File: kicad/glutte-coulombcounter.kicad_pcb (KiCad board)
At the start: 2 copper layers, 85 x 50 mm, 59 parts, among them J1 12V, J2 Measure, J3 I2C, J4 AVR-ISP-6, J5 DB9_Female, U1 DS18B20, U2 LT1236-5, U3 LT3433, U4 AD8210, U5 LTC2400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

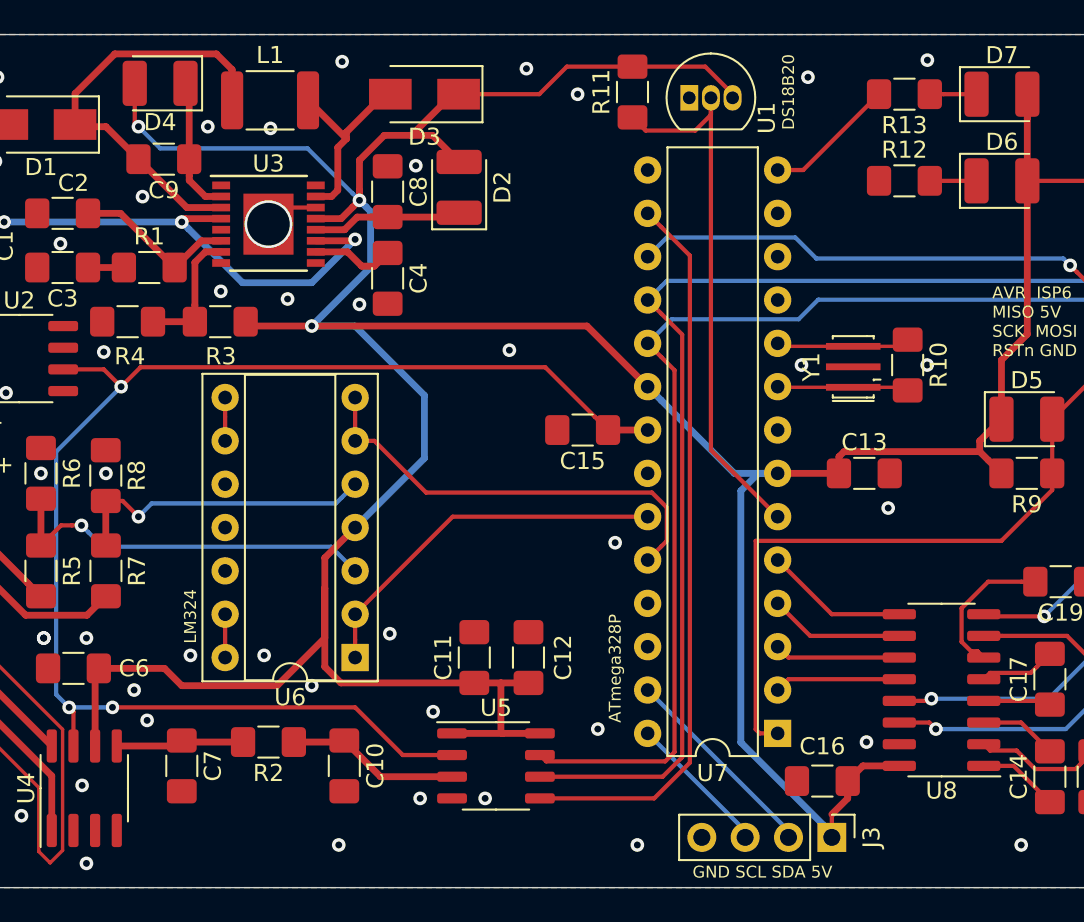
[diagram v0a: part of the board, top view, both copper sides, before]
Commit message: Change LM324 footprint to SOIC
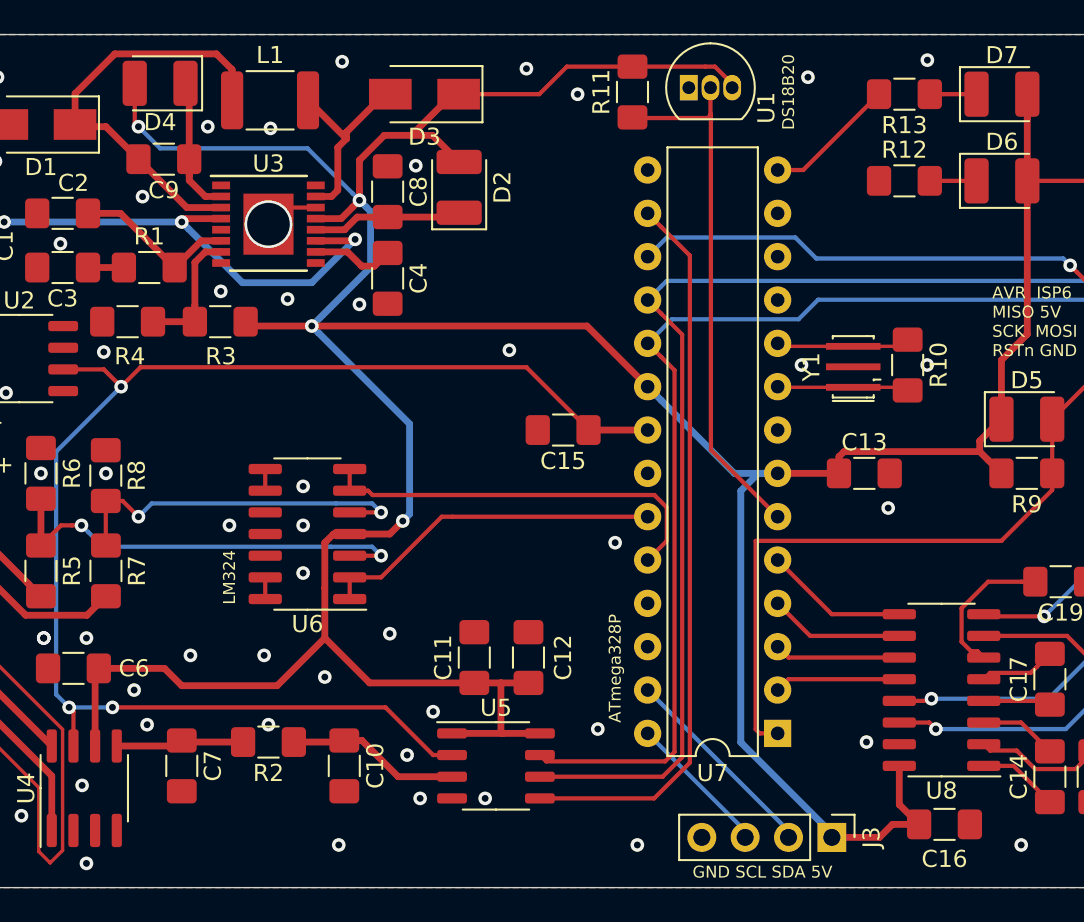
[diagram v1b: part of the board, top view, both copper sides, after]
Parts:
- U6: footprint Package_DIP:DIP-14_W7.62mm_Socket -> Package_SO:SOIC-14_3.9x8.7mm_P1.27mm
- moved U6 7.76 mm to (58.2, 49.3)
- moved C16 7.60 mm to (95.5, 66.3), turned to 0 degrees
- moved C15 1.14 mm to (73.2, 43.2)
- moved U1 0.60 mm to (80.5, 23.1)
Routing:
- net Net-(R7-Pad1): track 18.4 -> 21.5 mm, vias 1 -> 2
- net Net-(R5-Pad1): track 22.7 -> 25.7 mm, vias 1 -> 2
- net /ADC1: track 26.0 -> 23.8 mm
- net +5VA: track 246.7 -> 244.7 mm, vias 3 -> 4
- net /ADC0: track 22.1 -> 20.2 mm
- net Net-(U6-Pad8): track 2.54 -> 1.27 mm
- net Net-(U6-Pad13): track 2.54 -> 1.27 mm
- net /1WIRE: track 32.5 -> 31.5 mm
- net GNDA: vias 60 -> 66

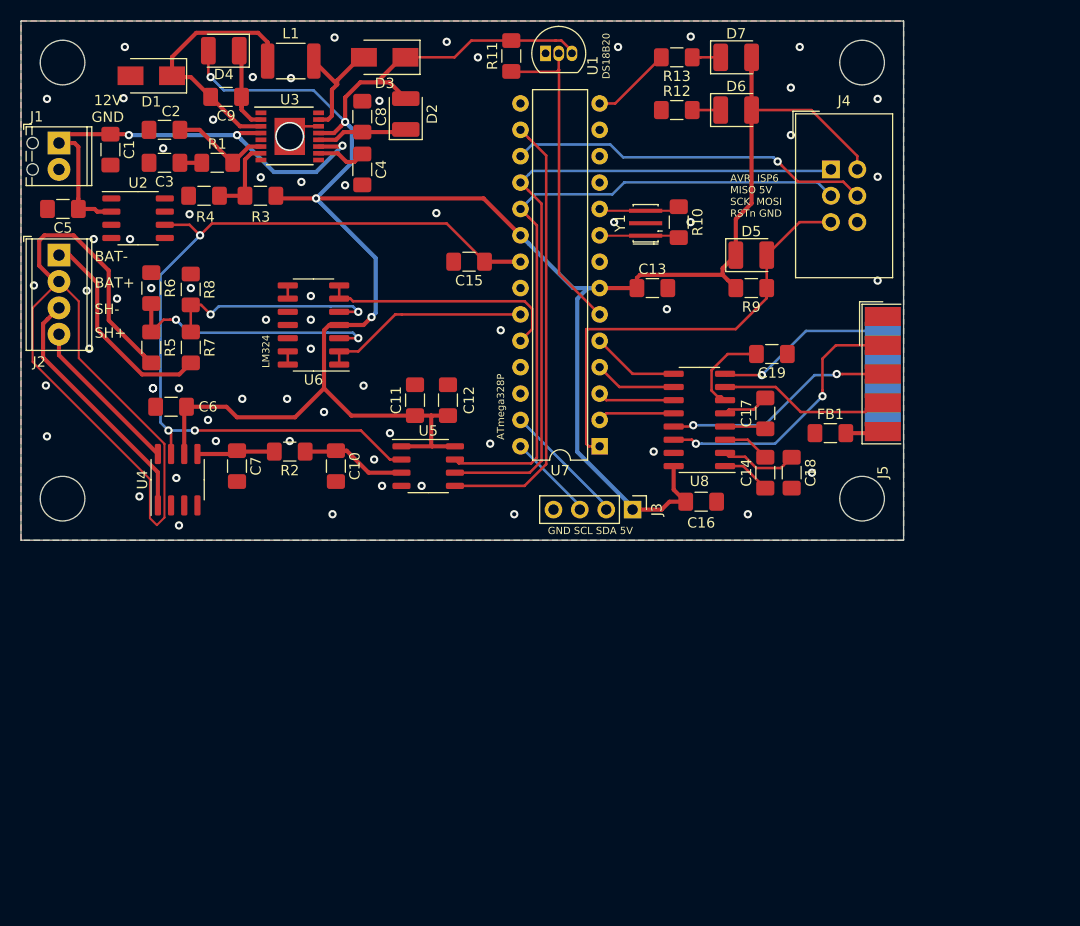
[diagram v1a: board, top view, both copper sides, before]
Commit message: Rework some routing
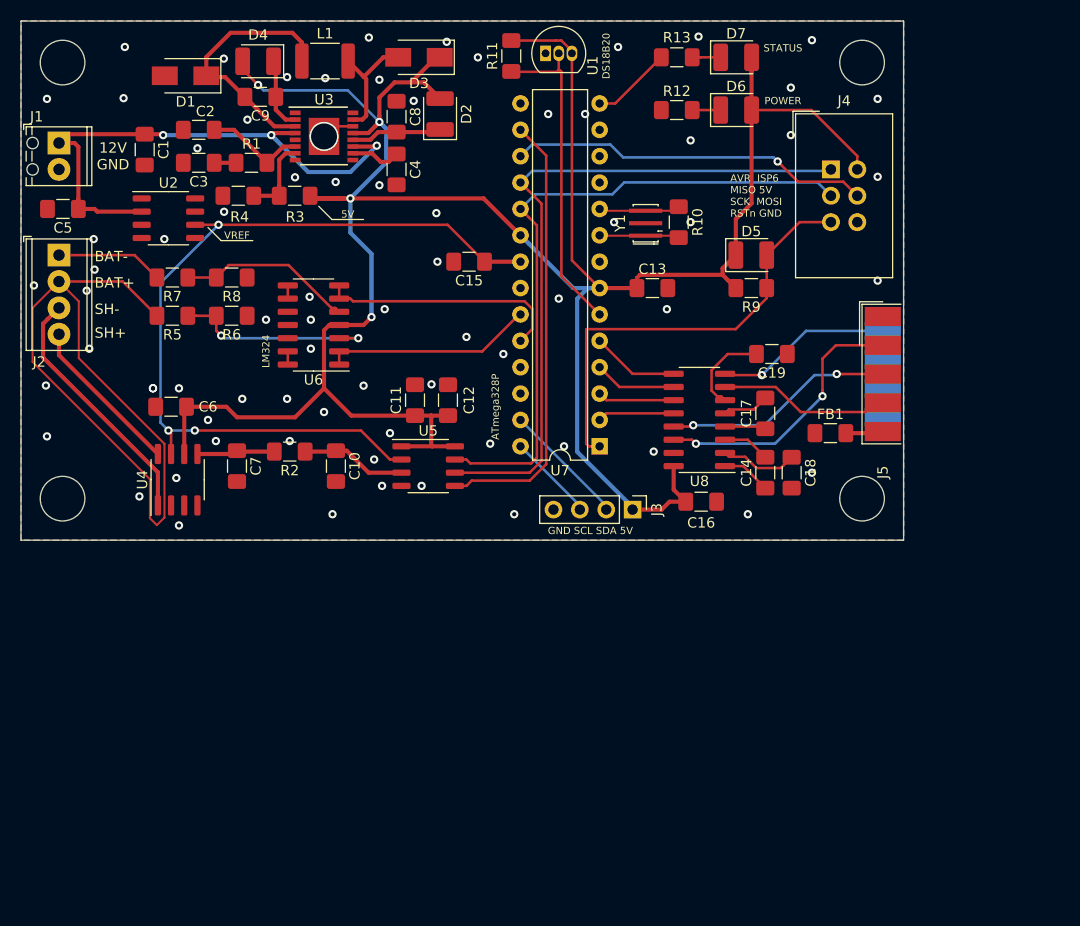
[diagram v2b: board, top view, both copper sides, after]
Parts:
- moved R6 8.19 mm to (50.3, 48.4), turned to 180 degrees
- moved R7 6.96 mm to (44.6, 44.7), turned to 180 degrees
- moved R8 4.11 mm to (50.3, 44.7), turned to 180 degrees
- moved R5 3.66 mm to (44.6, 48.4), turned to 180 degrees
- moved D4 3.45 mm to (52.8, 23.9)
- moved D2 3.30 mm to (70.4, 29.0)
- moved C1 3.30 mm to (41.9, 32.4)
- moved C2 3.30 mm to (47.1, 30.5)
- moved C3 3.30 mm to (47.1, 33.7)
- moved C4 3.30 mm to (66.2, 34.3)
- moved C8 3.30 mm to (66.2, 29.2)
- moved C9 3.30 mm to (53.0, 27.3)
- moved D1 3.30 mm to (45.8, 25.3)
- moved L1 3.30 mm to (59.3, 23.9)
- moved R1 3.30 mm to (52.2, 33.7)
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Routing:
- net +BATT: track 81.3 -> 68.3 mm
- net +5VA: track 244.7 -> 255.6 mm
- net -BATT: track 20.6 -> 10.3 mm
- net +12V: track 46.2 -> 52.5 mm
- net Net-(R5-Pad1): track 25.7 -> 20.0 mm
- net Net-(R7-Pad1): track 21.5 -> 16.9 mm, vias 2 -> 0
- net VREF: track 83.4 -> 81.2 mm
- net GNDA: vias 66 -> 74
- net (no net): vias 0 -> 1
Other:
- board text added: "5V"
- board text added: "POWER"
- board text added: "STATUS"
- board text added: "VREF"

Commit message: Update TODO, minor routing
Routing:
- net /SCK: track 64.4 -> 63.4 mm
- net GNDA: vias 74 -> 78
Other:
- board text added: "Coulombmetre Batterie Glutte Aout 2019 HB9EGM"
- board text removed: "Coulombmetre Batterie Glutte Juillet 2019 HB9EGM"

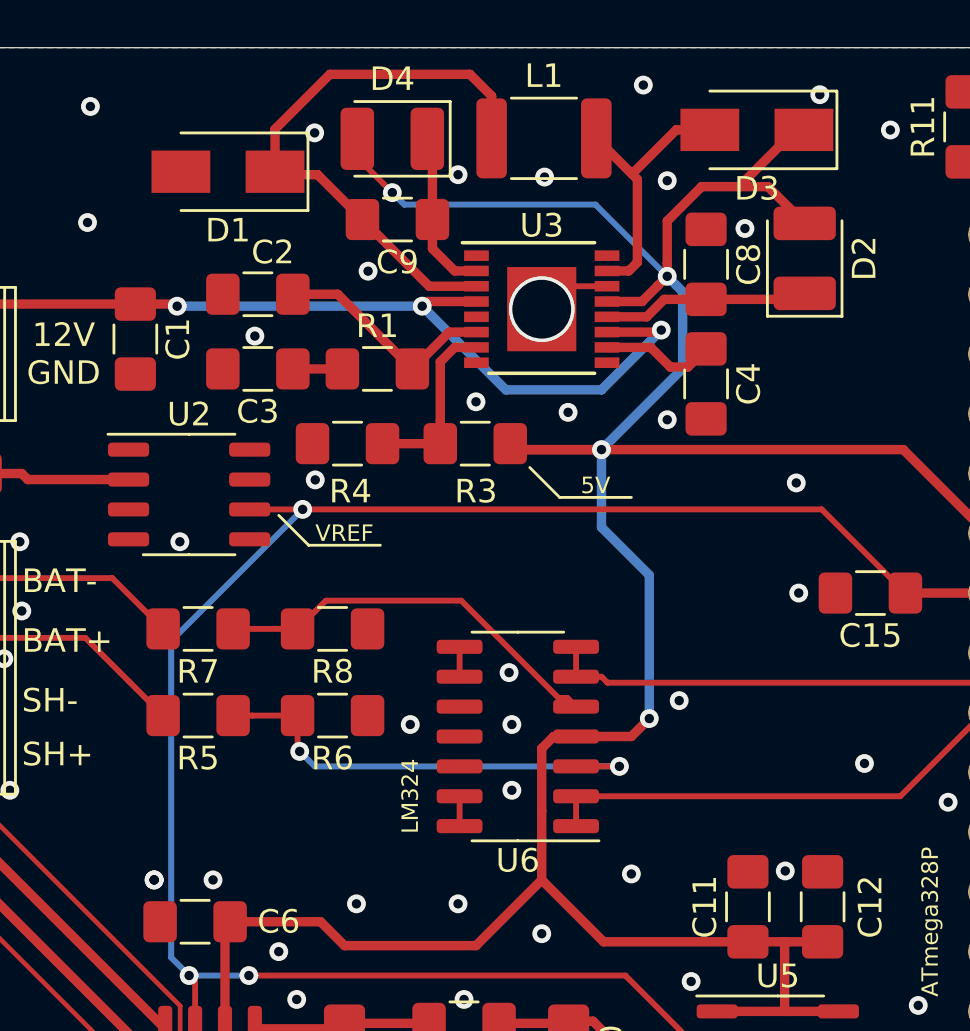
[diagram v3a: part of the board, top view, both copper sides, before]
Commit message: Move power supply to separate sheet
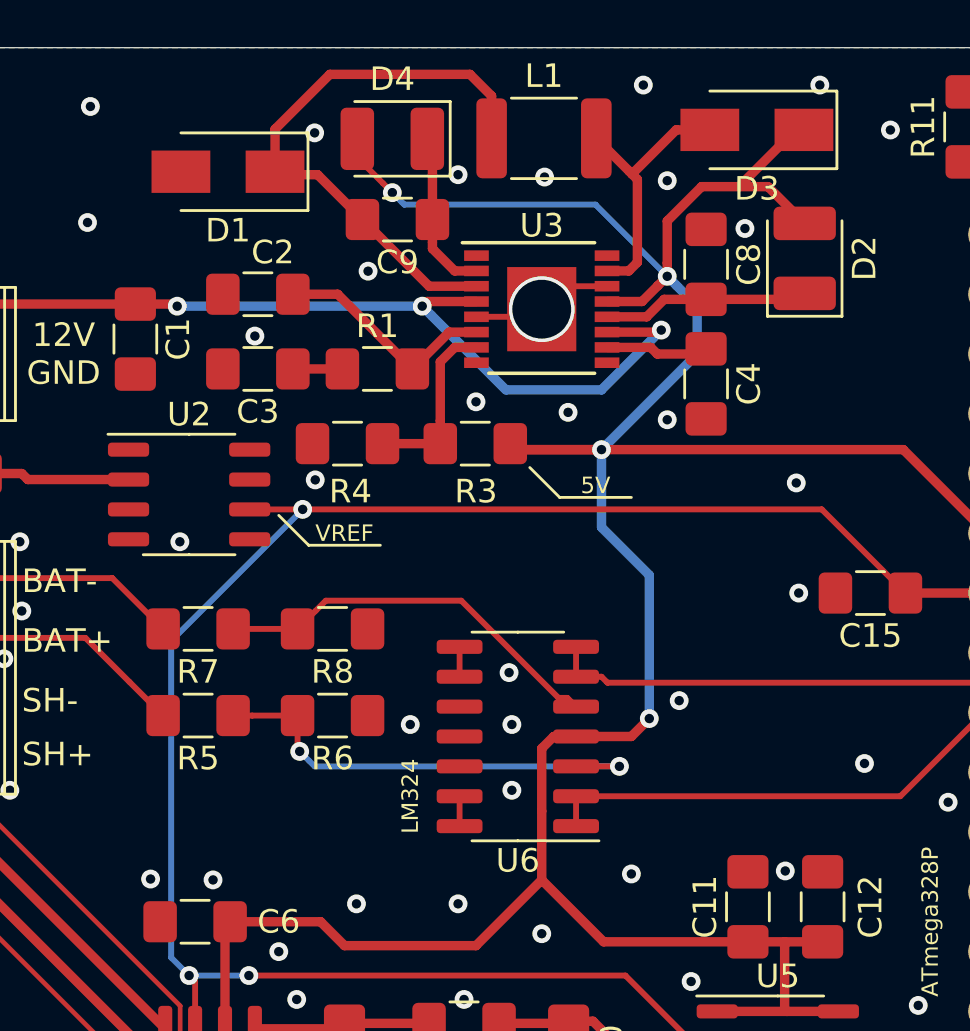
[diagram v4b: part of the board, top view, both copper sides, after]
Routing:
- net GNDA: track 3.18 -> 6.09 mm, vias 78 -> 77
- net +5VA: track 255.6 -> 256.1 mm
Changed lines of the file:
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@@
     (thickness 1.6)
     (drawings 54)
-    (tracks 446)
+    (tracks 447)
     (zones 0)
     (modules 59)
@@
     (34 B.Paste user hide)
     (35 F.Paste user hide)
-    (36 B.SilkS user hide)
+    (36 B.SilkS user)
     (37 F.SilkS user)
     (38 B.Mask user hide)
@@
     (effects (font (size 0.7 0.7) (thickness 0.1)))
   )
-  (gr_text "Concu avec KiCad" (at 69.596 26.162 180) (layer B.SilkS)
+  (gr_text "Concu avec KiCad" (at 69.7103 24.7142 180) (layer B.SilkS)
     (effects (font (size 1 1) (thickness 0.15)) (justify mirror))
   )
@@
   (via (at 87.5 22.5) (size 0.8) (drill 0.4) (layers F.Cu B.Cu) (net 1))
   (via (at 74 23.5) (size 0.8) (drill 0.4) (layers F.Cu B.Cu) (net 1))
-  (via (at 71 22) (size 0.8) (drill 0.4) (layers F.Cu B.Cu) (net 1))
+  (via (at 71 21.59) (size 0.8) (drill 0.4) (layers F.Cu B.Cu) (net 1))
   (via (at 63.5 21.59) (size 0.8) (drill 0.4) (layers F.Cu B.Cu) (net 1))
   (via (at 40 22.5) (size 0.8) (drill 0.4) (layers F.Cu B.Cu) (net 1))
@@
   (via (at 37.084 43.942) (size 0.8) (drill 0.4) (layers F.Cu B.Cu) (net 1))
   (via (at 36.322 45.974) (size 0.8) (drill 0.4) (layers F.Cu B.Cu) (net 1))
-  (via (at 42.708988 55.372) (size 0.8) (drill 0.4) (layers F.Cu B.Cu) (net 1))
-  (via (at 42.70899 55.372) (size 0.8) (drill 0.4) (layers F.Cu B.Cu) (net 1))
+  (via (at 42.5577 55.3339) (size 0.8) (drill 0.4) (layers F.Cu B.Cu) (net 1))
   (via (at 67.818 27.686) (size 0.8) (drill 0.4) (layers F.Cu B.Cu) (net 1))
   (via (at 64.008 62.23) (size 0.8) (drill 0.4) (layers F.Cu B.Cu) (net 1))
@@
   (via (at 84.074 33.02) (size 0.8) (drill 0.4) (layers F.Cu B.Cu) (net 1))
   (via (at 84.074 35.56) (size 0.8) (drill 0.4) (layers F.Cu B.Cu) (net 1))
+  (segment (start 58.857 31.44) (end 59.182 31.115) (width 0.25) (layer F.Cu) (net 1))
+  (segment (start 56.407 31.44) (end 58.857 31.44) (width 0.25) (layer F.Cu) (net 1))
   (via (at 64.262 32.004) (size 0.8) (drill 0.4) (layers F.Cu B.Cu) (net 2))
   (segment (start 64.176 32.09) (end 64.262 32.004) (width 0.4) (layer F.Cu) (net 2))
@@
   (segment (start 53.6845 33.655) (end 50.5095 30.48) (width 0.4) (layer F.Cu) (net 3))
   (segment (start 50.7095 33.655) (end 48.6045 33.655) (width 0.4) (layer F.Cu) (net 4))
-  (segment (start 63.813996 32.74) (end 64.647843 33.573847) (width 0.4) (layer F.Cu) (net 5))
+  (segment (start 64.093996 33.02) (end 65.9495 33.02) (width 0.4) (layer F.Cu) (net 5))
   (segment (start 61.957 32.74) (end 63.813996 32.74) (width 0.4) (layer F.Cu) (net 5))
-  (segment (start 64.647843 33.573847) (end 65.395653 33.573847) (width 0.4) (layer F.Cu) (net 5))
-  (segment (start 65.395653 33.573847) (end 66.167 32.8025) (width 0.4) (layer F.Cu) (net 5))
+  (segment (start 65.9495 33.02) (end 66.167 32.8025) (width 0.4) (layer F.Cu) (net 5))
+  (segment (start 63.813996 32.74) (end 64.093996 33.02) (width 0.4) (layer F.Cu) (net 5))
   (via (at 61.722 37.084) (size 0.8) (drill 0.4) (layers F.Cu B.Cu) (net 6))
   (segment (start 58.0985 37.084) (end 57.8445 36.83) (width 0.4) (layer F.Cu) (net 6))
@@
   (segment (start 65.974744 25.908) (end 64.516004 27.36674) (width 0.4) (layer F.Cu) (net 6))
   (segment (start 64.516004 29.152315) (end 64.516004 29.718) (width 0.4) (layer F.Cu) (net 6))
-  (segment (start 64.916003 30.117999) (end 64.516004 29.718) (width 0.4) (layer B.Cu) (net 6))
-  (segment (start 65.169999 33.636001) (end 65.169999 30.371995) (width 0.4) (layer B.Cu) (net 6))
   (segment (start 64.516004 27.36674) (end 64.516004 29.152315) (width 0.4) (layer F.Cu) (net 6))
-  (segment (start 61.722 37.084) (end 65.169999 33.636001) (width 0.4) (layer B.Cu) (net 6))
   (segment (start 67.563 25.908) (end 65.974744 25.908) (width 0.4) (layer F.Cu) (net 6))
   (segment (start 63.444004 30.79) (end 64.116005 30.117999) (width 0.4) (layer F.Cu) (net 6))
-  (segment (start 65.169999 30.371995) (end 64.916003 30.117999) (width 0.4) (layer B.Cu) (net 6))
   (via (at 63.754 48.514) (size 0.8) (drill 0.4) (layers F.Cu B.Cu) (net 6))
   (segment (start 60.641 49.276) (end 62.992 49.276) (width 0.4) (layer F.Cu) (net 6))
@@
   (segment (start 64.516004 29.718) (end 61.468004 26.67) (width 0.25) (layer B.Cu) (net 6))
   (segment (start 52.431995 25.762001) (end 52.831994 26.162) (width 0.25) (layer F.Cu) (net 6))
+  (segment (start 64.916003 30.117999) (end 64.516004 29.718) (width 0.4) (layer B.Cu) (net 6))
+  (segment (start 61.722 37.084) (end 65.786 33.02) (width 0.4) (layer B.Cu) (net 6))
+  (segment (start 65.786 30.987996) (end 64.916003 30.117999) (width 0.4) (layer B.Cu) (net 6))
+  (segment (start 65.786 33.02) (end 65.786 30.987996) (width 0.4) (layer B.Cu) (net 6))
   (segment (start 50.4775 61.7) (end 50.8 61.3775) (width 0.4) (layer F.Cu) (net 7))
   (segment (start 46.99 61.7) (end 50.4775 61.7) (width 0.4) (layer F.Cu) (net 7))
